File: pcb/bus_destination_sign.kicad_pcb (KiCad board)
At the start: 2 copper layers, 50 x 32.5 mm, 34 parts, among them J1 USB_C_Receptacle_USB2.0_16P, J2 Display Connector Input, J3 SSD1322 30-Pin Connector, U1 ESP32-S3-WROOM-1, U2 AP2112K-3.3, U3 MT3608

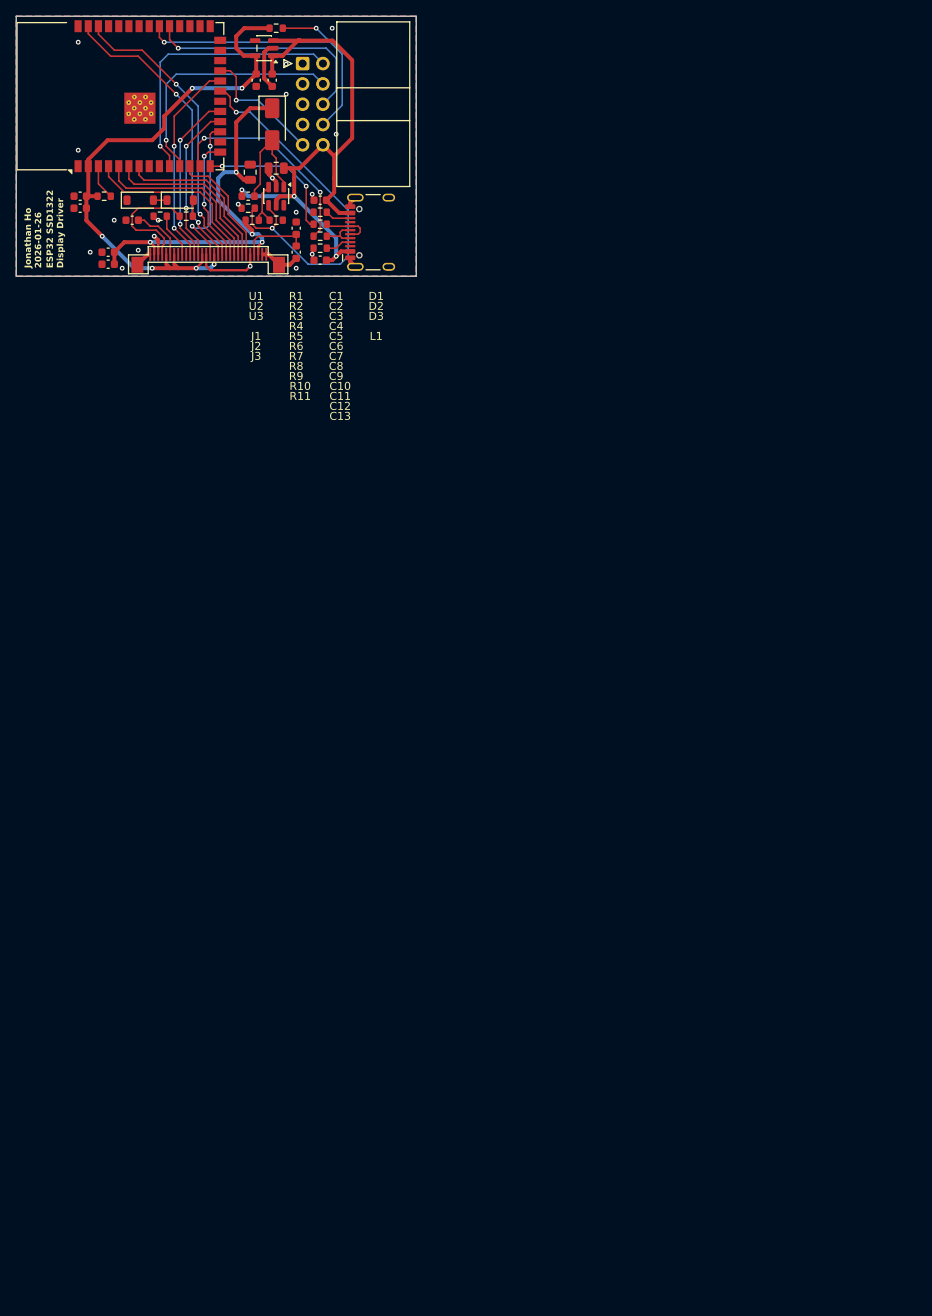
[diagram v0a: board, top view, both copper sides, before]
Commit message: Added ESP32 master circuit
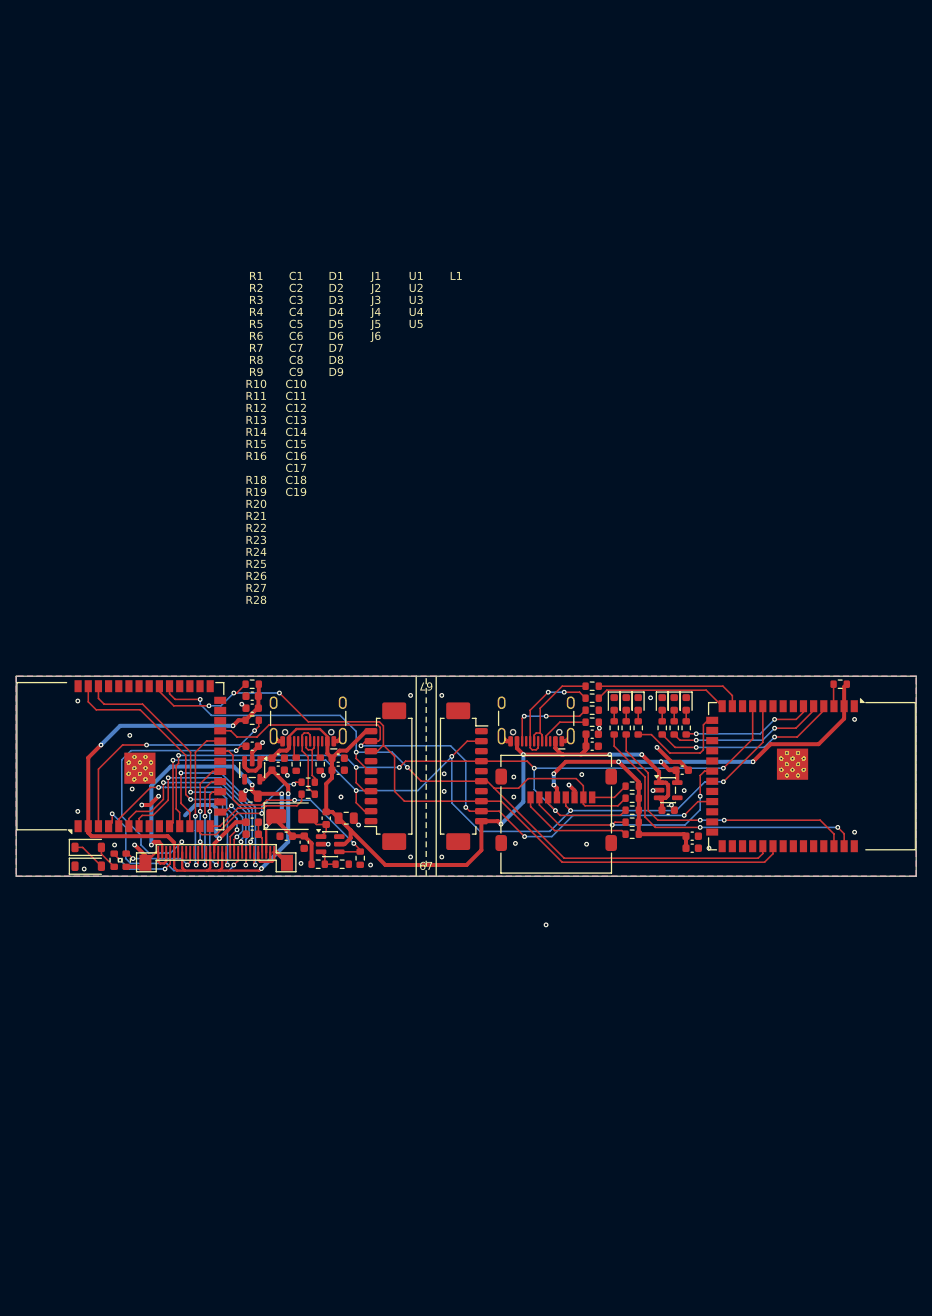
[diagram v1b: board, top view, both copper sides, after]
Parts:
- added C14: 1uF, Capacitor_SMD:C_0603_1608Metric, F.Cu at (82.8, 160.2)
- added C15: 2.2uF, Capacitor_SMD:C_0603_1608Metric, F.Cu at (82.8, 161.8)
- added C16: 10uF, Capacitor_SMD:C_0603_1608Metric, F.Cu at (90.2, 160.2)
- added C17: 0.1uF, Capacitor_SMD:C_0603_1608Metric, F.Cu at (90.2, 161.8)
- added C18: 10uF, Capacitor_SMD:C_0603_1608Metric, F.Cu at (79.5, 152.5)
- added C19: 0.1uF, Capacitor_SMD:C_0603_1608Metric, F.Cu at (79.5, 154.0)
- added D4: Red LED, LED_SMD:LED_0603_1608Metric, F.Cu at (124.8, 153.5)
- added D5: Yellow LED, LED_SMD:LED_0603_1608Metric, F.Cu at (126.2, 153.5)
- added D6: Green LED, LED_SMD:LED_0603_1608Metric, F.Cu at (127.8, 153.5)
- added D7: Red LED, LED_SMD:LED_0603_1608Metric, F.Cu at (130.8, 153.5)
- added D8: Yellow LED, LED_SMD:LED_0603_1608Metric, F.Cu at (132.2, 153.5)
- added D9: Green LED, LED_SMD:LED_0603_1608Metric, F.Cu at (133.8, 153.5)
- added J4: USB_C_Receptacle_USB2.0_16P, Connector_USB:USB_C_Receptacle_HCTL_HC-TYPE-C-16P-01A, F.Cu at (115.0, 154.4)
- added J5: Display Connector Output, Connector_Molex:Molex_PicoBlade_53261-1071_1x10-1MP_P1.25mm_Horizontal, F.Cu at (105.8, 162.5)
- added J6: Micro_SD_Card, Connector_Card:microSD_HC_Molex_47219-2001, F.Cu at (117.5, 167.2)
- added R12: 5.1k, Resistor_SMD:R_0603_1608Metric, F.Cu at (85.0, 161.0)
- added R13: 5.1k, Resistor_SMD:R_0603_1608Metric, F.Cu at (88.0, 161.0)
- added R14: 22R, Resistor_SMD:R_0603_1608Metric, F.Cu at (86.5, 163.2)
- added R15: 22R, Resistor_SMD:R_0603_1608Metric, F.Cu at (86.5, 164.8)
- added R16: 10k, Resistor_SMD:R_0603_1608Metric, F.Cu at (79.5, 155.5)
- added R18: 10k, Resistor_SMD:R_0603_1608Metric, F.Cu at (127.0, 169.8)
- added R19: 10k, Resistor_SMD:R_0603_1608Metric, F.Cu at (127.0, 166.8)
- added R20: 10k, Resistor_SMD:R_0603_1608Metric, F.Cu at (127.0, 165.2)
- added R21: 10k, Resistor_SMD:R_0603_1608Metric, F.Cu at (127.0, 163.8)
- added R22: 10k, Resistor_SMD:R_0603_1608Metric, F.Cu at (127.0, 168.2)
- added R23: 470R, Resistor_SMD:R_0603_1608Metric, F.Cu at (124.8, 156.5)
- added R24: 470R, Resistor_SMD:R_0603_1608Metric, F.Cu at (126.2, 156.5)
- added R25: 470R, Resistor_SMD:R_0603_1608Metric, F.Cu at (127.8, 156.5)
- added R26: 470R, Resistor_SMD:R_0603_1608Metric, F.Cu at (130.8, 156.5)
- added R27: 470R, Resistor_SMD:R_0603_1608Metric, F.Cu at (132.2, 156.5)
- added R28: 470R, Resistor_SMD:R_0603_1608Metric, F.Cu at (133.8, 156.5)
- added U4: AP2112K-3.3, Package_TO_SOT_SMD:SOT-23-5, F.Cu at (131.5, 164.2)
- added U5: ESP32-S3-WROOM-1, RF_Module:ESP32-S3-WROOM-1, F.Cu at (149.5, 162.5)
- C1: value 10uF -> 1uF
- C12: value 1uF -> 10uF
- C13: value 2.2uF -> 0.1uF
- C2: value 0.1uF -> 2.2uF
- J2: footprint Connector_IDC:IDC-Header_2x05_P2.54mm_Horizontal -> Connector_Molex:Molex_PicoBlade_53261-1071_1x10-1MP_P1.25mm_Horizontal
- moved C13 110.4 mm to (134.5, 171.5), turned to 0 degrees
- moved R11 110.4 mm to (153.0, 151.0), turned to 180 degrees
- moved C12 108.1 mm to (134.5, 170.0), turned to 0 degrees
- moved C1 106.3 mm to (131.5, 166.8), turned to 0 degrees
- moved C2 102.9 mm to (133.2, 161.8), turned to 0 degrees
- moved U2 90.3 mm to (79.5, 161.8), turned to -90 degrees
- moved J2 89.8 mm to (96.8, 162.5), turned to 90 degrees
- moved D3 86.5 mm to (84.5, 167.5), turned to 0 degrees
- moved D2 83.5 mm to (59.0, 173.8)
- moved U1 82.5 mm to (63.0, 160.0)
- moved R9 82.4 mm to (93.0, 172.8), turned to -90 degrees
- moved R10 82.1 mm to (79.5, 151.0), turned to 180 degrees
- moved C8 81.7 mm to (91.2, 167.8), turned to 0 degrees
- moved D1 81.7 mm to (59.0, 171.4)
- moved U3 81.3 mm to (89.2, 171.0), turned to 0 degrees
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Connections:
- net Net-(J2-CLK) renamed /CLK
- net Net-(J2-CS) renamed /CS_DISPLAY
- net Net-(J2-MISO) renamed /MISO
- net Net-(J2-MOSI) renamed /MOSI
- net Net-(J2-WAKE) renamed /WAKE
- net Net-(J3-CS#) renamed /ESP32 for SSD1322/GPIO11
- net Net-(J3-D0) renamed /ESP32 for SSD1322/GPIO1
- net Net-(J3-D1) renamed /ESP32 for SSD1322/GPIO2
- net Net-(J3-D2) renamed /ESP32 for SSD1322/GPIO3
- net Net-(J3-D3) renamed /ESP32 for SSD1322/GPIO4
- net Net-(J3-D4) renamed /ESP32 for SSD1322/GPIO5
- net Net-(J3-D5) renamed /ESP32 for SSD1322/GPIO6
- net Net-(J3-D6) renamed /ESP32 for SSD1322/GPIO7
- net Net-(J3-D7) renamed /ESP32 for SSD1322/GPIO8
- net Net-(J3-DC#) renamed /ESP32 for SSD1322/GPIO10
- net Net-(J3-RES#) renamed /ESP32 for SSD1322/GPIO14
- net Net-(J3-RW#) renamed /ESP32 for SSD1322/GPIO9
- net Net-(U1-IO13) renamed /ESP32 for SSD1322/GPIO13
- C1 pad 1: +3V3 -> +5V
- C12 pad 1: +5V -> +3V3
- R11 pad 2: Net-(U1-EN) -> Net-(U5-EN)
- R5 pad 1: Net-(J1-CC2) -> Net-(J4-CC2)
- R6 pad 1: Net-(J1-CC1) -> Net-(J4-CC1)
- R7 pad 1: Net-(J1-D--PadA7) -> Net-(J4-D--PadA7)
- R7 pad 2: Net-(U1-USB_D-) -> Net-(U5-USB_D-)
- R8 pad 1: Net-(J1-D+-PadA6) -> Net-(J4-D+-PadA6)
- R8 pad 2: Net-(U1-USB_D+) -> Net-(U5-USB_D+)
- U1 pad 20: unconnected-(U1-IO12-Pad20) -> /ESP32 for SSD1322/GPIO12
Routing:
- net +3V3: track 72.4 -> 154.2 mm, vias 6 -> 9
- net /MISO: track 29.9 -> 110.0 mm, vias 1 -> 3
- net /MOSI: track 31.6 -> 109.8 mm, vias 1 -> 6
- net /CLK: track 34.7 -> 112.1 mm, vias 1 -> 5
- net /WAKE: track 15.9 -> 79.1 mm, vias 1 -> 4
- net /CS_DISPLAY: track 41.6 -> 96.7 mm, vias 2 -> 3
- net /Master ESP32/GPIO1: track 0.00 -> 39.2 mm, vias 0 -> 2
- net /Master ESP32/GPIO2: track 0.00 -> 36.6 mm, vias 0 -> 2
- net /CS_SD: track 0.00 -> 30.7 mm, vias 0 -> 2
- net +5V: track 75.8 -> 104.7 mm, vias 3 -> 4
- net Net-(J3-VDD): track 6.93 -> 35.5 mm, vias 0 -> 2
- net Net-(U1-EN): track 4.39 -> 30.2 mm, vias 0 -> 2
- net /Master ESP32/GPIO4: track 0.00 -> 23.3 mm, vias 0 -> 2
- net GND: track 29.9 -> 50.4 mm, vias 19 -> 41
- net /Master ESP32/GPIO5: track 0.00 -> 19.8 mm, vias 0 -> 2
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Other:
- board size 50 x 32.5 mm -> 112.5 x 25 mm
- board text added: "67"
- board text added: "ESP32 1:13 RC Bus System"
- board text added: "Jonathan Ho 2026-01-27"
- board text removed: "Jonathan Ho 2026-01-26"

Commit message: Updated LED footprints
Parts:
- D4, D5, D6, D7, D8, D9: footprint LED_SMD:LED_0603_1608Metric -> LED_SMD:LED_0805_2012Metric
- moved D6 0.78 mm to (128.5, 153.2)
- moved D9 0.78 mm to (134.5, 153.2)
- moved D4 0.33 mm to (124.5, 153.2)
- moved D5 0.33 mm to (126.5, 153.2)
- moved D7 0.33 mm to (130.5, 153.2)
- moved D8 0.33 mm to (132.5, 153.2)
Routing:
- net Net-(U5-USB_D+): track 16.7 -> 15.8 mm

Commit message: Fixed 3.3V connections and SD card orientation
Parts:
- turned J6 to 180 degrees
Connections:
- C12 pad 1: +3V3 -> /Master ESP32/3V3
- C13 pad 1: +3V3 -> /Master ESP32/3V3
- C15 pad 1: +3V3 -> /ESP32 for SSD1322/3V3
- C18 pad 1: +3V3 -> /ESP32 for SSD1322/3V3
- C19 pad 1: +3V3 -> /ESP32 for SSD1322/3V3
- C2 pad 1: +3V3 -> /Master ESP32/3V3
- J2 pad MP: (no net) -> GND
- J3 pad 14: +3V3 -> /ESP32 for SSD1322/3V3
- J3 pad 17: +3V3 -> /ESP32 for SSD1322/3V3
- J3 pad 24: +3V3 -> /ESP32 for SSD1322/3V3
- J3 pad 26: +3V3 -> /ESP32 for SSD1322/3V3
- J5 pad MP: (no net) -> GND
- J6 pad 4: +3V3 -> /Master ESP32/3V3
- R10 pad 1: +3V3 -> /ESP32 for SSD1322/3V3
- R11 pad 1: +3V3 -> /Master ESP32/3V3
- R16 pad 1: +3V3 -> /ESP32 for SSD1322/3V3
- R18 pad 1: +3V3 -> /Master ESP32/3V3
- R19 pad 1: +3V3 -> /Master ESP32/3V3
- R20 pad 1: +3V3 -> /Master ESP32/3V3
- R21 pad 1: +3V3 -> /Master ESP32/3V3
- R22 pad 1: +3V3 -> /Master ESP32/3V3
- U1 pad 2: +3V3 -> /ESP32 for SSD1322/3V3
- U2 pad 5: +3V3 -> /ESP32 for SSD1322/3V3
- U4 pad 5: +3V3 -> /Master ESP32/3V3
- U5 pad 2: +3V3 -> /Master ESP32/3V3
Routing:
- net +3V3: track 154.2 -> 0.00 mm, vias 9 -> 0
- net /ESP32 for SSD1322/3V3: track 0.00 -> 85.9 mm, vias 0 -> 4
- net /Master ESP32/3V3: track 0.00 -> 69.5 mm, vias 0 -> 3
- net Net-(J6-DAT1): track 4.76 -> 16.1 mm
- net Net-(J6-DAT2): track 14.5 -> 5.64 mm
- net /MOSI: track 109.8 -> 107.0 mm
- net /CS_SD: track 30.7 -> 28.0 mm
- net /CS_DISPLAY: track 96.7 -> 99.2 mm
- net +5V: track 104.7 -> 106.6 mm
- net GND: track 50.4 -> 48.6 mm, vias 41 -> 38
- net /WAKE: track 79.1 -> 77.7 mm
- net (no net): vias 1 -> 0
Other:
- board text added: "Jonathan Ho 2026-01-28"
- board text removed: "Jonathan Ho 2026-01-27"
